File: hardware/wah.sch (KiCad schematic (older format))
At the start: 17 parts

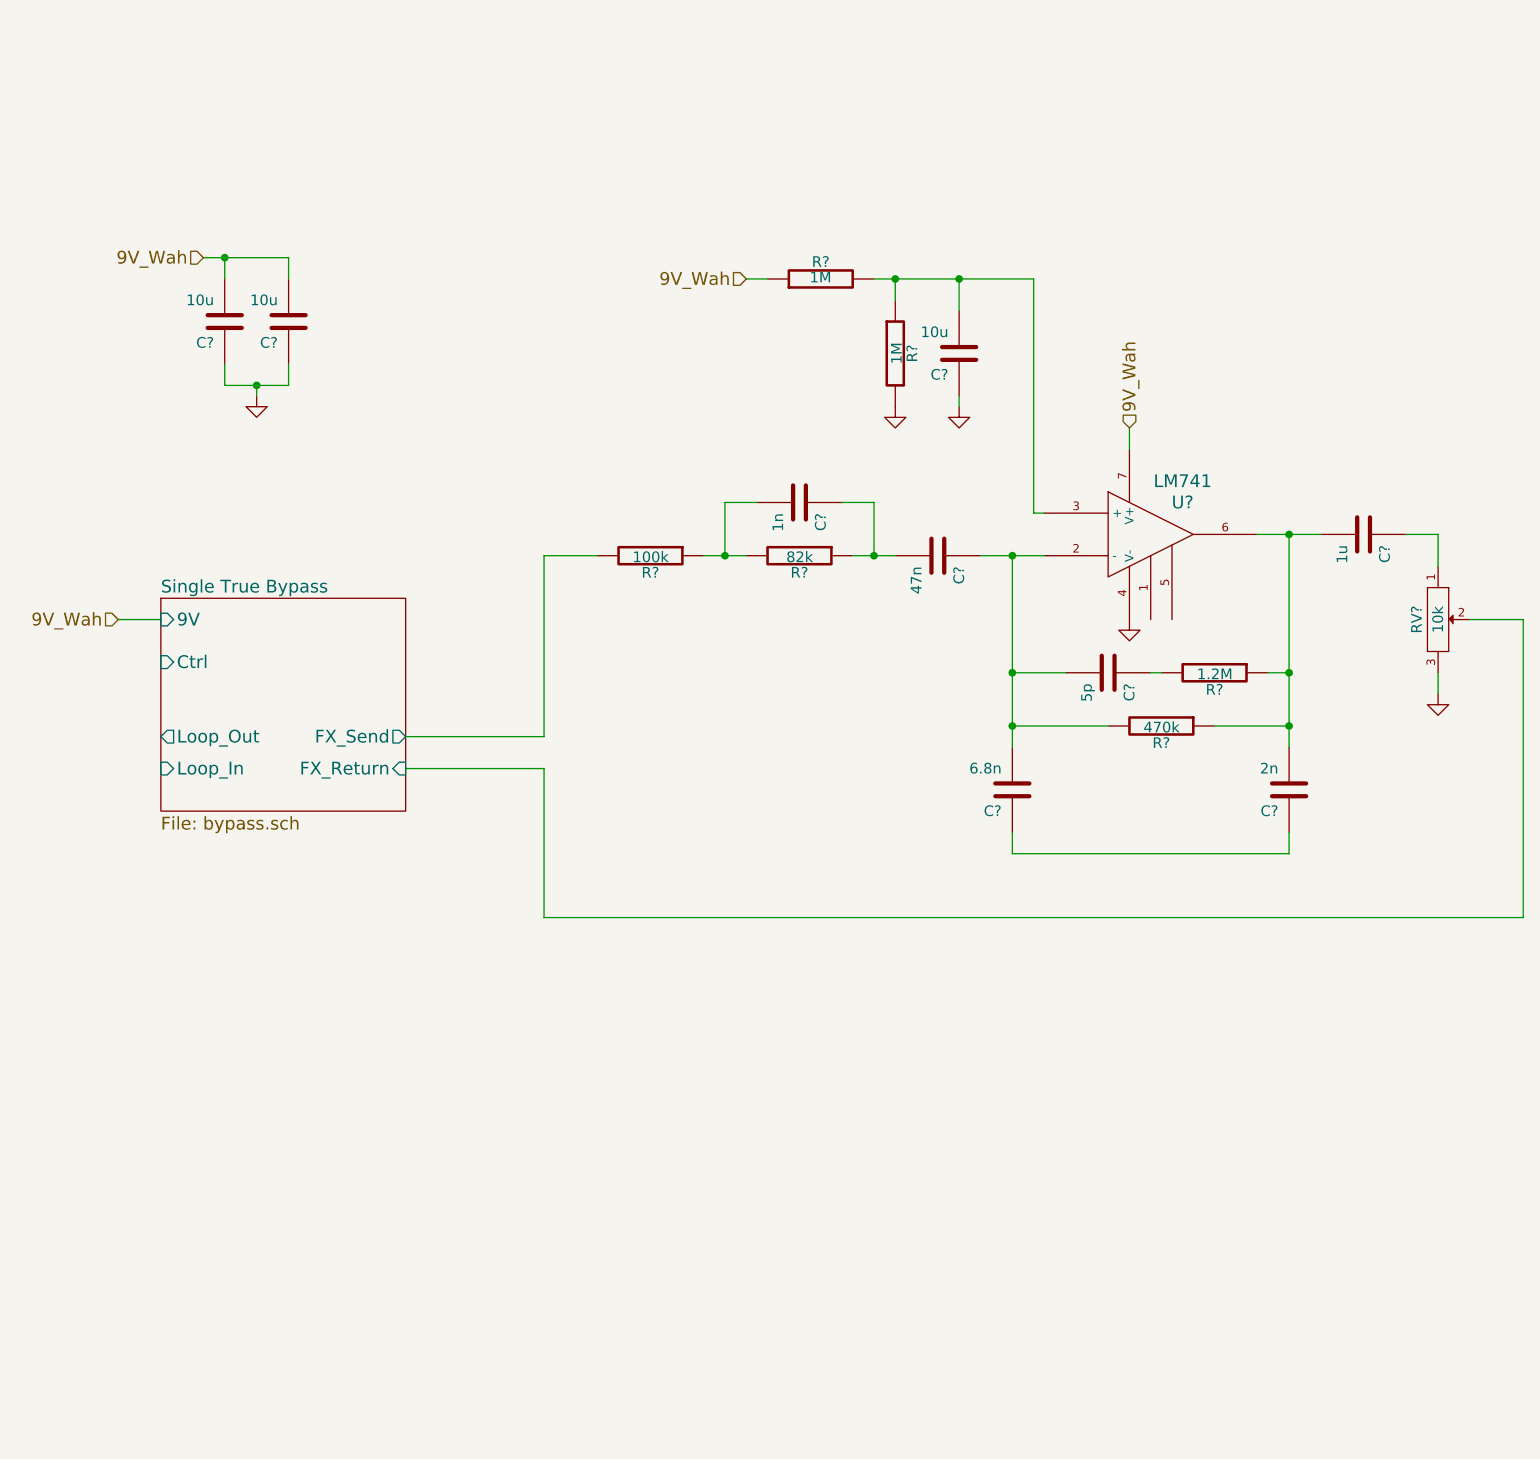
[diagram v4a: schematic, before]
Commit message: Complete wah circuit
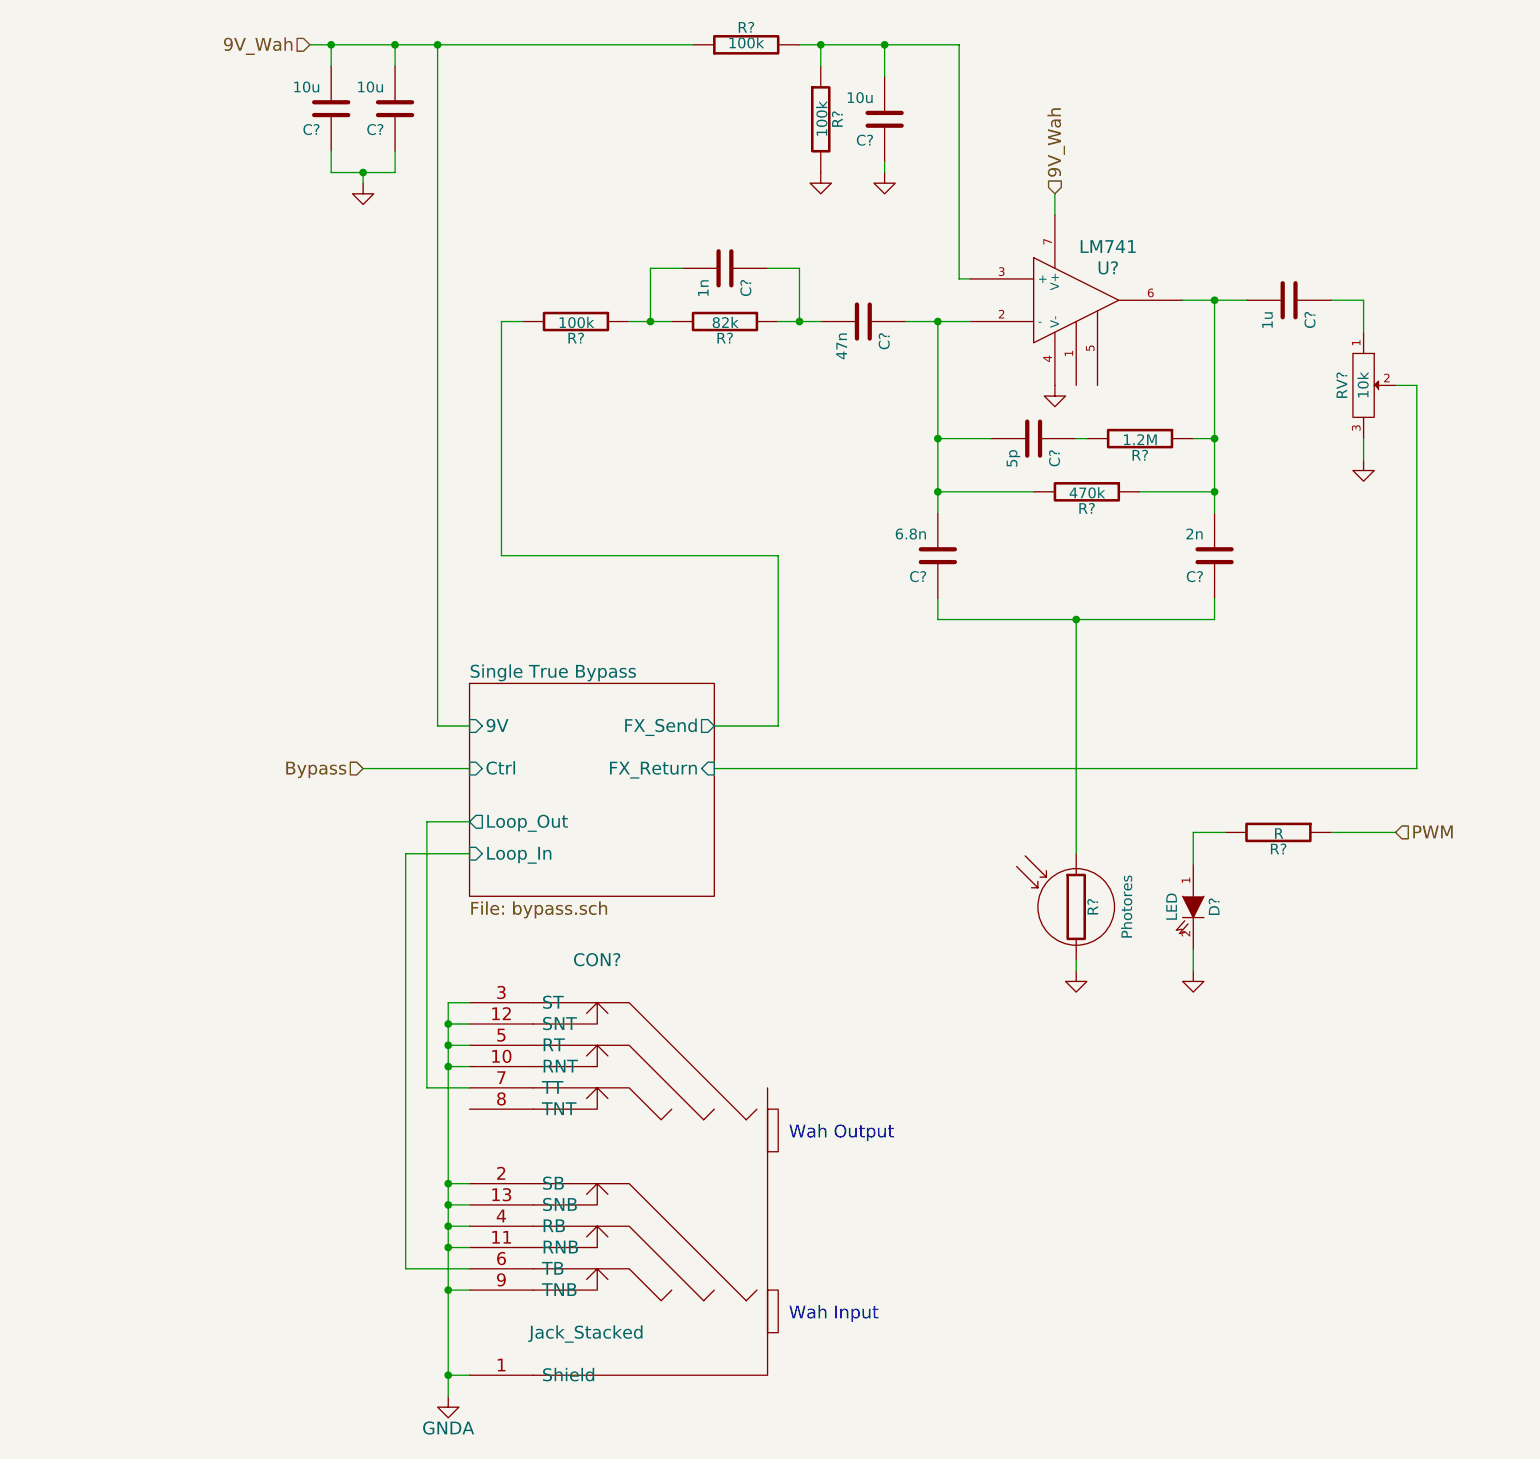
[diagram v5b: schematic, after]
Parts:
- added CON?: Jack_Stacked, symbol Jack_Stacked
- added D?: LED, symbol LED
- added R?: Photores, symbol Photores
- added R?: R, symbol R
- R? (x2): value 1M -> 100k
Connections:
- net GND: now also D?.2 (K), R?.2
- net Single True Bypass/Loop_In: now also CON?.6 (TB)
- net Single True Bypass/Loop_Out: now also CON?.7 (TT)
- net at C?.1, C?.1: now also R?.1
- new net: D?.1 (A), R?.2
- new net GNDA: CON?.1 (Shield), CON?.10 (RNT), CON?.11 (RNB), CON?.12 (SNT), CON?.13 (SNB), CON?.2 (SB), CON?.3 (ST), CON?.4 (RB), CON?.5 (RT), CON?.9 (TNB)
- new net PWM: R?.1
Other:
- note added: "Wah Input"
- note added: "Wah Output"
- moved on the sheet: C?, R?, RV?, U?

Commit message: Use global label for digital (noisy) 9V
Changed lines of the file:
@@
 F4 "FX_Send" O R 4300 4200 60
 F5 "FX_Return" I R 4300 4400 60
-F6 "9V" I L 3150 4200 60
 F7 "Ctrl" I L 3150 4400 60
 $EndSheet
@@
 Wire Wire Line
 	7600 4400 4300 4400
-Wire Wire Line
-	3150 4200 3000 4200
-Wire Wire Line
-	3000 4200 3000 1000
 Connection ~ 2800 1000
-Connection ~ 3000 1000
 Wire Wire Line
 	2950 4650 3150 4650
